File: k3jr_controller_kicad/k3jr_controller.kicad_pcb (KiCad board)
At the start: 2 copper layers, 161.3 x 40.6 mm, 80 parts, among them J1 CLK_IN, J17 MISO, J18 3V3, J19 SCK, J2 DAT_IN, J20 SPI, J21 MOSI, J22 RST, J23 GND, J24 I2C_ext1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

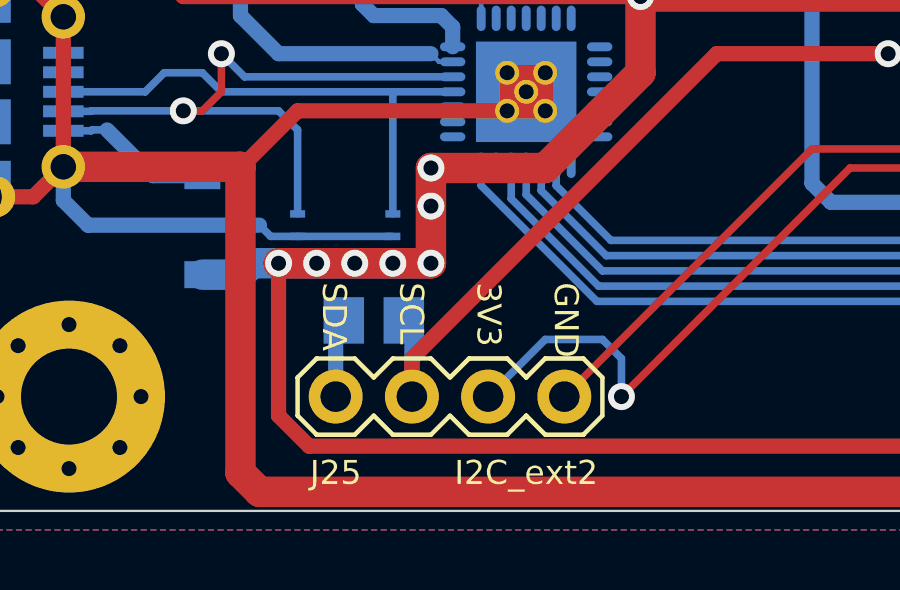
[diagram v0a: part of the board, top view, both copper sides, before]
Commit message: corrected I2C silk legend
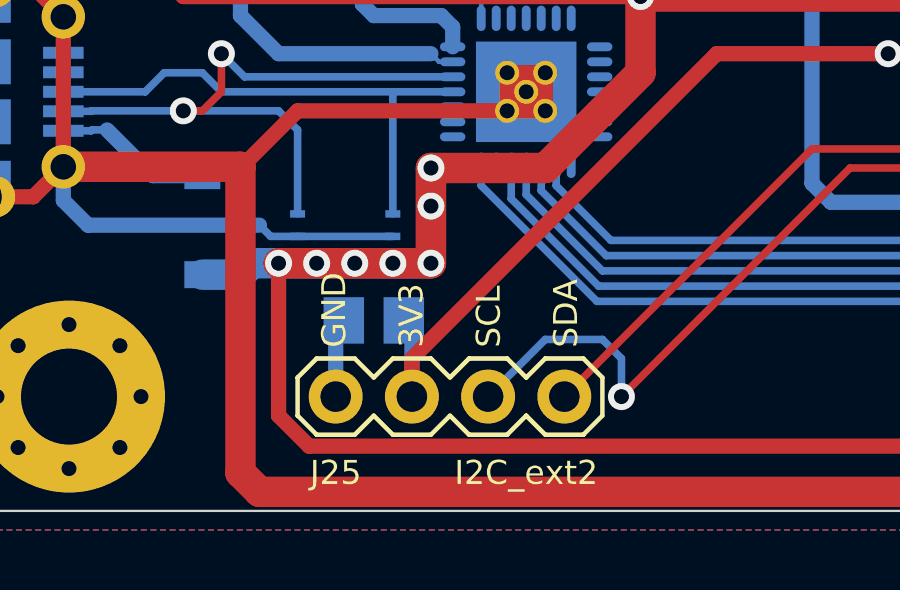
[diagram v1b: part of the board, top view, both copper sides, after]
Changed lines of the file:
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@@
-(kicad_pcb (version 20171130) (host pcbnew no-vcs-found-3ad3869~61~ubuntu16.04.1)
+(kicad_pcb (version 20171130) (host pcbnew no-vcs-found-67ccf76~61~ubuntu16.04.1)
   (general
     (thickness 1.6)
@@
     (visible_elements 7FFFFF7F)
     (pcbplotparams
-      (layerselection 0x00130_ffffffff)
+      (layerselection 0x00030_7ffffffe)
       (usegerberextensions true)
       (usegerberattributes false)
       (usegerberadvancedattributes false)
       (creategerberjobfile false)
-      (excludeedgelayer false)
+      (excludeedgelayer true)
       (linewidth 0.150000)
-      (plotframeref true)
+      (plotframeref false)
       (viasonmask false)
       (mode 1)
@@
       (padsonsilk true)
       (subtractmaskfromsilk true)
-      (outputformat 4)
+      (outputformat 1)
       (mirror false)
-      (drillshape 2)
+      (drillshape 0)
       (scaleselection 1)
-      (outputdirectory k3jr_controller_pdf/))
+      (outputdirectory k3jr_controller_gerber/))
   )
   (net 0 "")
@@
     (effects (font (size 0.8 0.8) (thickness 0.15)))
   )
-  (gr_text "GND\n\n3V3\n\nSCL\n\nSDA" (at 67.945 83.82 270) (layer F.SilkS)
+  (gr_text "GND\n\n3V3\n\nSCL\n\nSDA" (at 67.945 86 90) (layer F.SilkS)
     (effects (font (size 0.8 0.8) (thickness 0.15)) (justify left))
   )
@@
     (effects (font (size 0.8 0.8) (thickness 0.15)) (justify left))
   )
-  (gr_text "GND\n\n3V3\n\nSCL\n\nSDA" (at 67.945 91.44 270) (layer B.SilkS)
+  (gr_text "GND\n\n3V3\n\nSCL\n\nSDA" (at 68 89 90) (layer B.SilkS)
     (effects (font (size 0.8 0.8) (thickness 0.15)) (justify left mirror))
   )

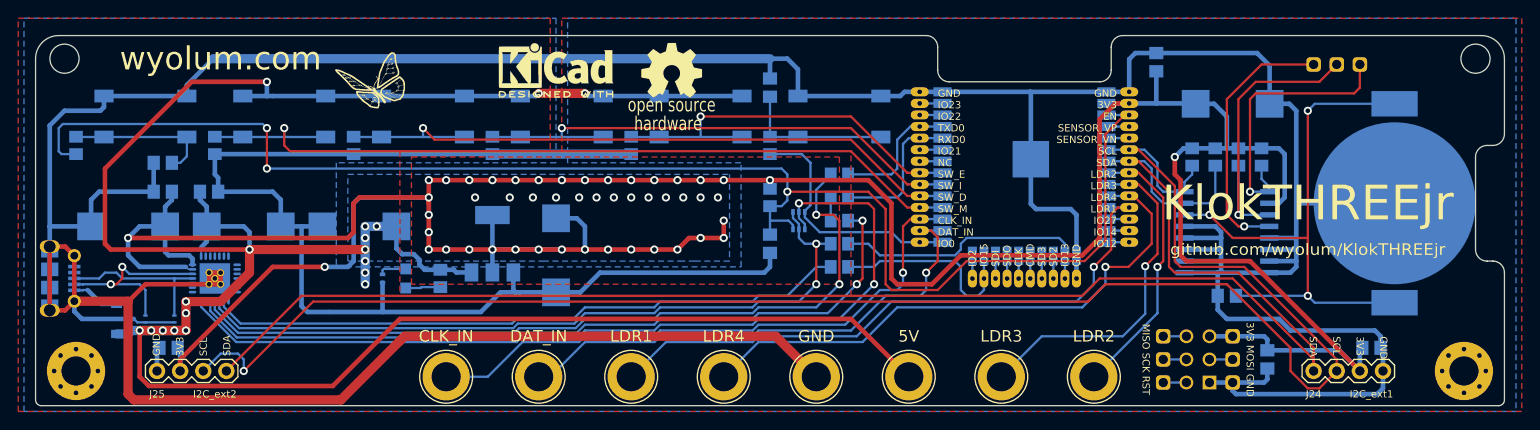
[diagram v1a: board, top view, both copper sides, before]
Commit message: changed I2C connections
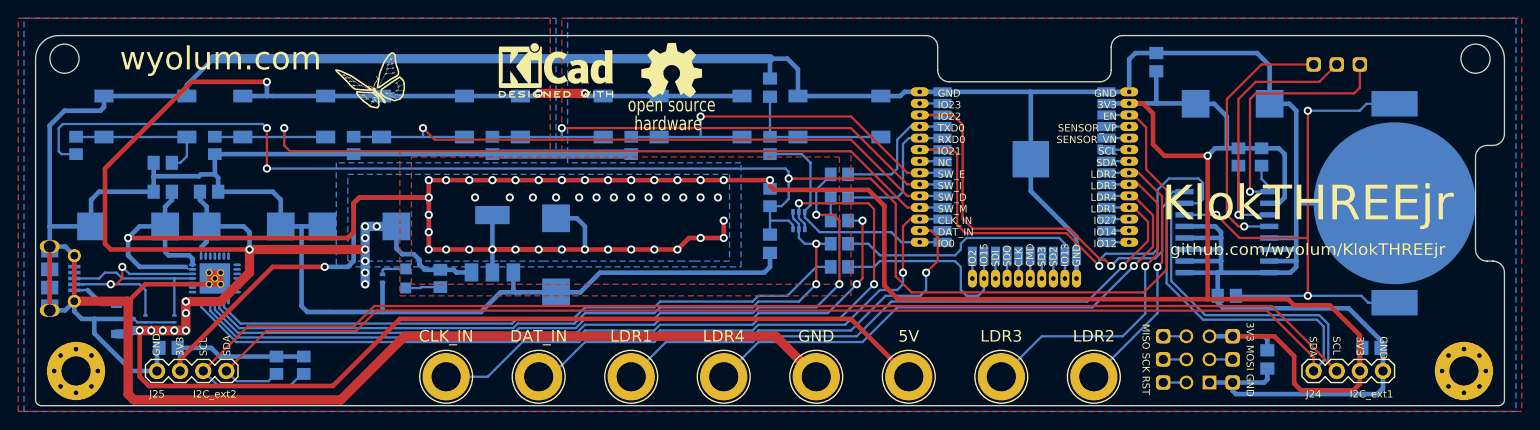
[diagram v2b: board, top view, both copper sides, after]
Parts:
- moved R8 103.1 mm to (77.2, 87.0)
- moved R9 102.7 mm to (80.2, 87.0)
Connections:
- J24 pad 1: /SDA -> /SCL
- J24 pad 2: /SCL -> /SDA
- J25 pad 1: /SDA -> /SCL
- J25 pad 2: /SCL -> /SDA
- P1 pad 4: (no net) -> Net-(P1-Pad4)
- U129 pad 33: /IO21 -> /SDA
- U129 pad 36: /IO22 -> /SCL
- U129 pad 6: /SCL -> Net-(U129-Pad6)
- U129 pad 7: /SDA -> Net-(U129-Pad7)
- U132 pad 1: (no net) -> /esp_pwr_uart/DCD
- U132 pad 10: (no net) -> Net-(U132-Pad10)
- U132 pad 11: (no net) -> /esp_pwr_uart/ACTIVE
- U132 pad 12: (no net) -> Net-(U132-Pad12)
- U132 pad 13: (no net) -> Net-(U132-Pad13)
- U132 pad 14: (no net) -> Net-(U132-Pad14)
- U132 pad 15: (no net) -> Net-(U132-Pad15)
- U132 pad 16: (no net) -> Net-(U132-Pad16)
- U132 pad 17: (no net) -> Net-(U132-Pad17)
- U132 pad 18: (no net) -> Net-(U132-Pad18)
- U132 pad 19: (no net) -> Net-(U132-Pad19)
- U132 pad 2: (no net) -> /esp_pwr_uart/RI
- U132 pad 20: (no net) -> Net-(U132-Pad20)
- U132 pad 21: (no net) -> Net-(U132-Pad21)
- U132 pad 22: (no net) -> Net-(U132-Pad22)
- U132 pad 27: (no net) -> /esp_pwr_uart/DSR
- U132 pad 9: (no net) -> Net-(U132-Pad9)
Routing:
- net /SDA: track 184.5 -> 233.0 mm, vias 0 -> 1
- net /3V3: track 368.2 -> 396.6 mm
- net /SCL: track 191.4 -> 218.9 mm
- net GND: track 630.6 -> 644.6 mm
- net /EN: track 164.5 -> 175.3 mm
- net Net-(U129-Pad7): track 0.00 -> 2.50 mm
- net Net-(U129-Pad6): track 0.00 -> 2.50 mm
- net /IO22: track 2.50 -> 0.00 mm
- net /IO21: track 2.50 -> 0.00 mm
- net /LDR1: track 68.3 -> 70.2 mm
- net /LDR4: track 63.2 -> 62.5 mm

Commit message: kontroller layout modified. Old layout archived as rev _v1
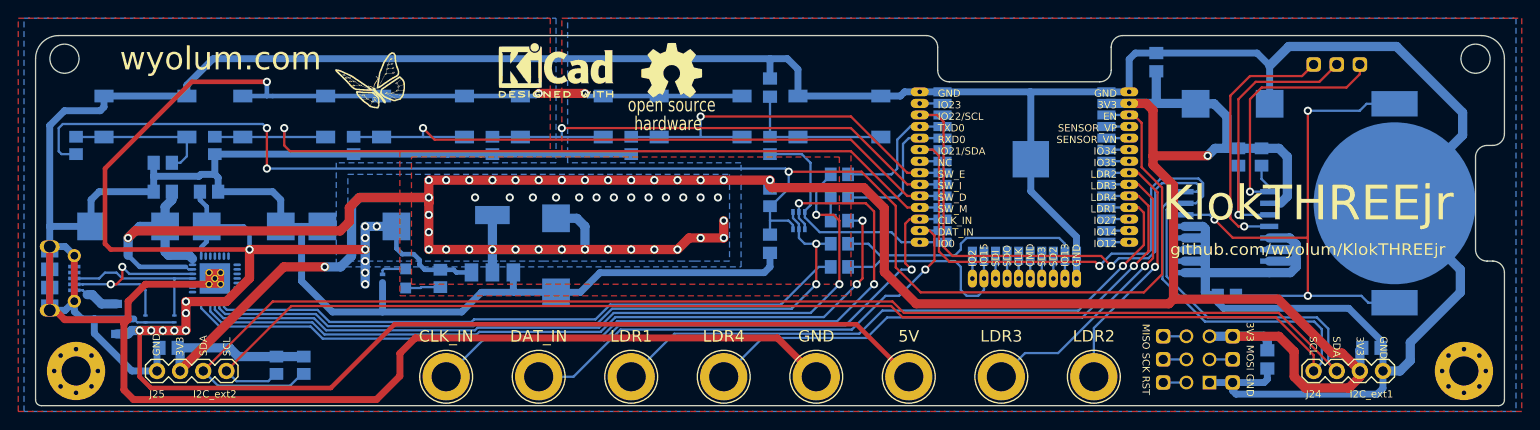
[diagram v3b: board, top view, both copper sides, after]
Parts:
- moved G1 4.37 mm to (92.0, 84.0)
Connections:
- net Net-(U129-Pad6) renamed /IO34
- net Net-(U129-Pad7) renamed /IO35
- P1 pad 4: Net-(P1-Pad4) -> (no net)
- U132 pad 1: /esp_pwr_uart/DCD -> (no net)
- U132 pad 10: Net-(U132-Pad10) -> (no net)
- U132 pad 11: /esp_pwr_uart/ACTIVE -> (no net)
- U132 pad 12: Net-(U132-Pad12) -> (no net)
- U132 pad 13: Net-(U132-Pad13) -> (no net)
- U132 pad 14: Net-(U132-Pad14) -> (no net)
- U132 pad 15: Net-(U132-Pad15) -> (no net)
- U132 pad 16: Net-(U132-Pad16) -> (no net)
- U132 pad 17: Net-(U132-Pad17) -> (no net)
- U132 pad 18: Net-(U132-Pad18) -> (no net)
- U132 pad 19: Net-(U132-Pad19) -> (no net)
- U132 pad 2: /esp_pwr_uart/RI -> (no net)
- U132 pad 20: Net-(U132-Pad20) -> (no net)
- U132 pad 21: Net-(U132-Pad21) -> (no net)
- U132 pad 22: Net-(U132-Pad22) -> (no net)
- U132 pad 27: /esp_pwr_uart/DSR -> (no net)
- U132 pad 9: Net-(U132-Pad9) -> (no net)
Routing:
- net GND: track 644.6 -> 678.0 mm
- net /SCL: track 218.9 -> 226.3 mm
- net /3V3: track 396.6 -> 393.0 mm
- net /LDR3: track 37.8 -> 34.3 mm
- net /DAT_IN: track 57.6 -> 55.8 mm
- net /SDA: track 233.0 -> 234.7 mm
- net /EN: track 175.3 -> 173.7 mm
- net /rtc_ds3231/32kHz: track 30.6 -> 29.7 mm
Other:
- net class 30mil added: clearance 0.2032, trace_width 0.762, via_dia 0.9, via_drill 0.5
- net class 40mil added: clearance 0.2032, trace_width 1.016, via_dia 0.9, via_drill 0.5
- net class 8 mil: clearance 0.0381 -> 0.1016
- net class Default: clearance 0.1016 -> 0.2032
- rule trace_clearance: 0.1016 -> 0.2032
- rule trace_min: 0.08 -> 0.1524
- rule via_min_size: 0.9 -> 0.762
- board text added: "GND 3V3 SDA SCL"
- board text added: "IO21/SDA"
- board text added: "IO22/SCL"
- board text added: "IO34"
- board text added: "IO35"
- board text removed: "GND 3V3 SCL SDA"
- board text removed: "IO21"
- board text removed: "IO22"
- board text removed: "SCL"
- board text removed: "SDA"
